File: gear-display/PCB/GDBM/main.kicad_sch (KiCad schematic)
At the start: 19 parts, among them U2 ATmega32U4-AU, X1 Programming_AVR_ISP_Staggered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, X2 CON_1x04_TH_staggered, Y1 Crystal_16M_AS-16.000-18-SMD-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

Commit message: fixes
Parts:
- D3: footprint KD_Diode:LED_0603_1608Metric_Pad1.05x0.95mm_HandSolder -> KD_Diode:DIOC1608X70

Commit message: Added a ferrite and silk screen markings
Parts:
- added FB?: Ferrite_250mA_Murata_BLM15HG102SN1D, KD_Inductor:INDC1005X55N, symbol KD_Inductor:Ferrite_250mA_Murata_BLM15HG102SN1D
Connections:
- net +5V: now also FB?.1; no longer C6.1, C7.2, C9.1, R2.1, R8.1, U2.14 (VCC), U2.2 (UVCC), U2.24 (AVCC), U2.34 (VCC1), U2.44 (AVCC1)
- new net: C6.1, C7.2, C9.1, FB?.2, R2.1, R8.1, U2.14 (VCC), U2.2 (UVCC), U2.24 (AVCC), U2.34 (VCC1), U2.44 (AVCC1)

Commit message: BOM generated
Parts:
- gave numbers to parts that had none: 1

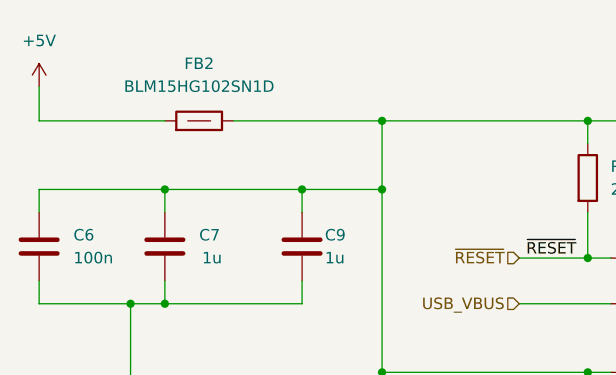
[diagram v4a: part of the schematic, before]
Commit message: led buffer added
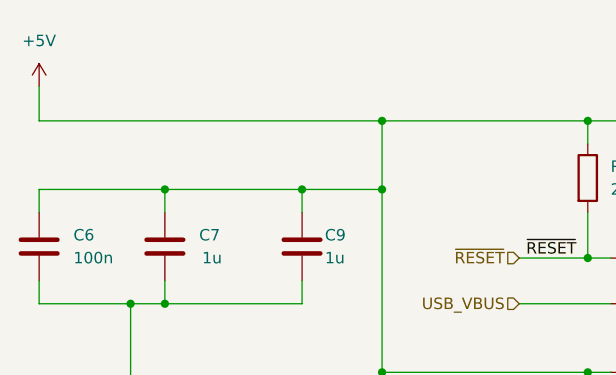
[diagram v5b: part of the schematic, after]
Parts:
- removed FB2: Ferrite_250mA_Murata_BLM15HG102SN1D, KD_Inductor:INDC1005X55N, symbol KD_Inductor:Ferrite_250mA_Murata_BLM15HG102SN1D
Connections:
- net +5V: now also C6.1, C7.2, C9.1, R2.1, R8.1, U2.14 (VCC), U2.2 (UVCC), U2.24 (AVCC), U2.34 (VCC1), U2.44 (AVCC1)

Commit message: change to kicad 7
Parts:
- D3: footprint KD_Diode:DIOC1608X70 -> KD_Diode:DIOC1608X70N
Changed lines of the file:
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@@
-(kicad_sch (version 20211123) (generator eeschema)
+(kicad_sch (version 20230121) (generator eeschema)
   (paper "A4")
   (title_block
